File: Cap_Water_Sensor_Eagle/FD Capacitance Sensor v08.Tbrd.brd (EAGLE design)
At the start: 35.1 x 27.6 mm, 17 parts, among them U1 NTS4101PT1, U2 TLC555CD

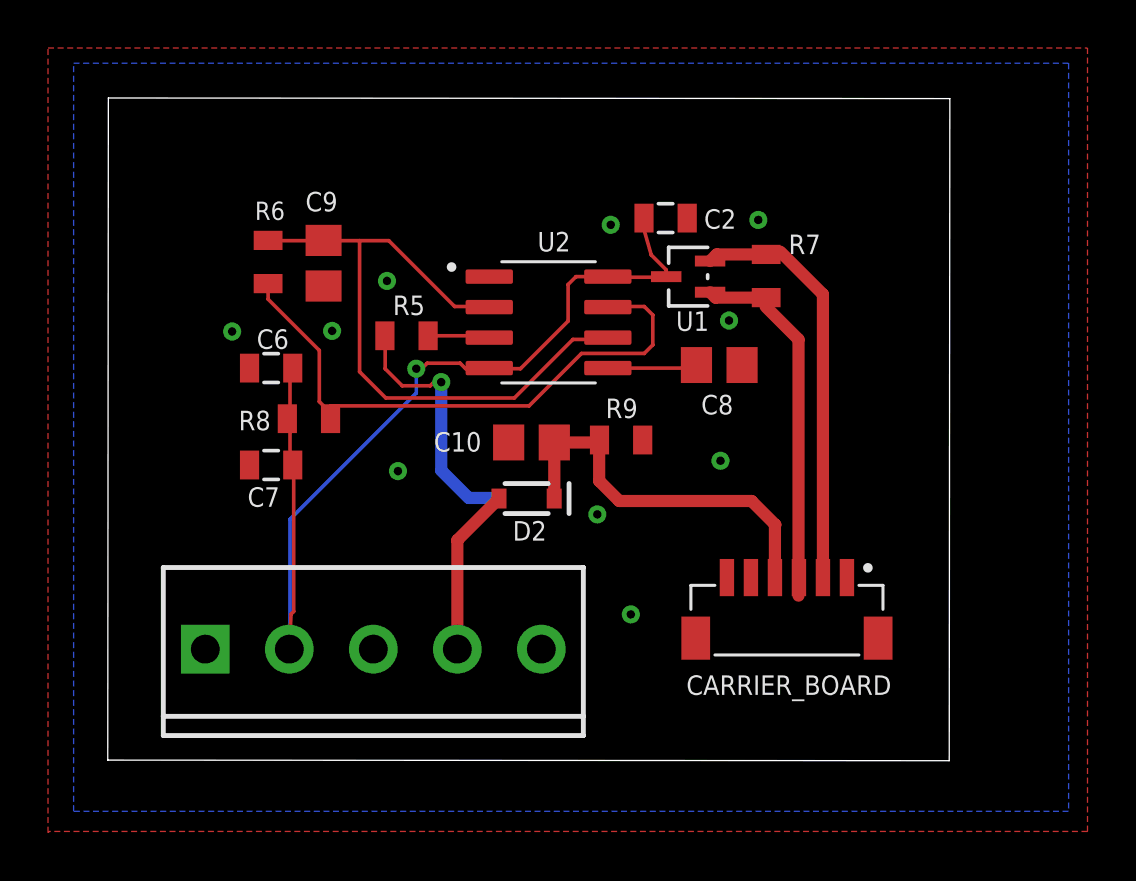
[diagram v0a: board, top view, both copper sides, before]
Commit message: Version 9 with board dimensions
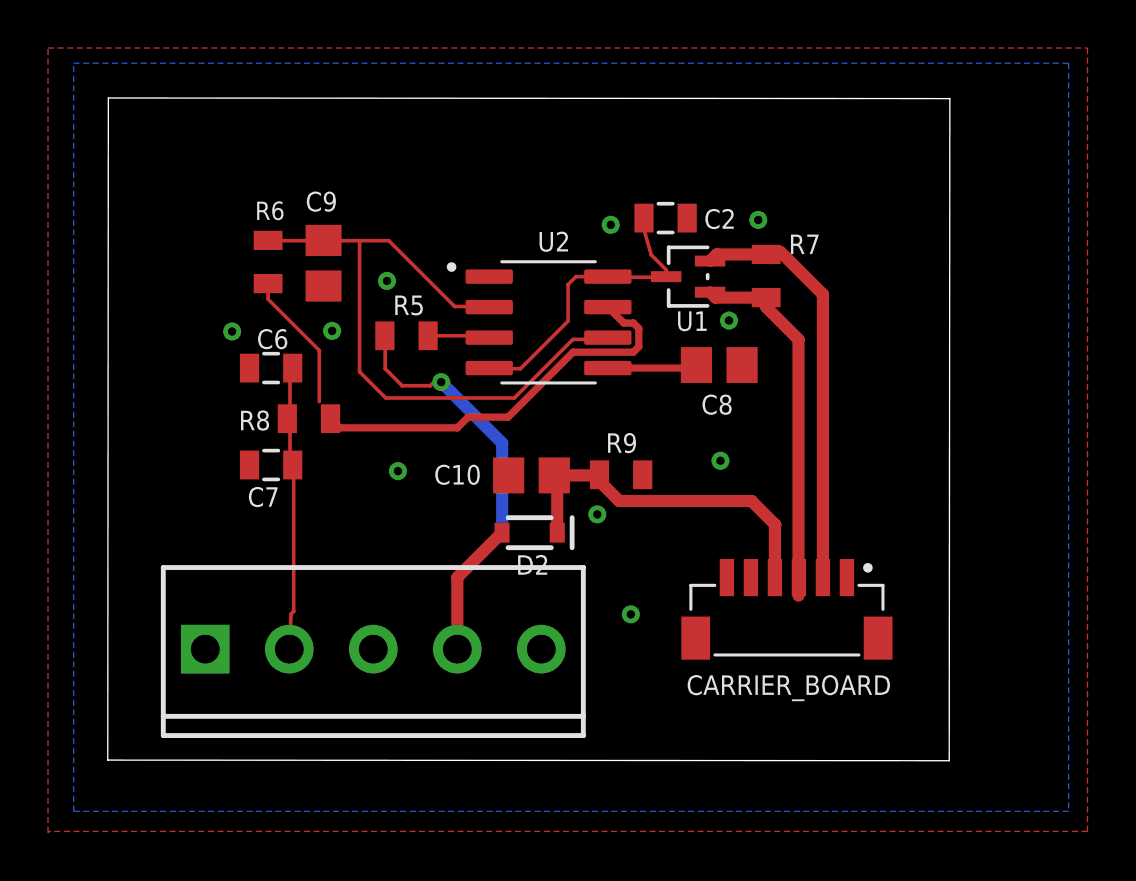
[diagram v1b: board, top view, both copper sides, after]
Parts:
- moved R9 1.45 mm to (21.4, 11.9)
- moved D2 1.43 mm to (17.6, 9.47)
- moved C10 1.37 mm to (17.7, 11.9)
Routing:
- net VCC: track 41.8 -> 24.6 mm, vias 1 -> 0
- net N$9: track 25.0 -> 22.6 mm
- net OUTPUT1: track 16.5 -> 15.2 mm
- net SENSOR1: track 17.6 -> 17.0 mm
